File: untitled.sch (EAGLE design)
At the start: 21 parts

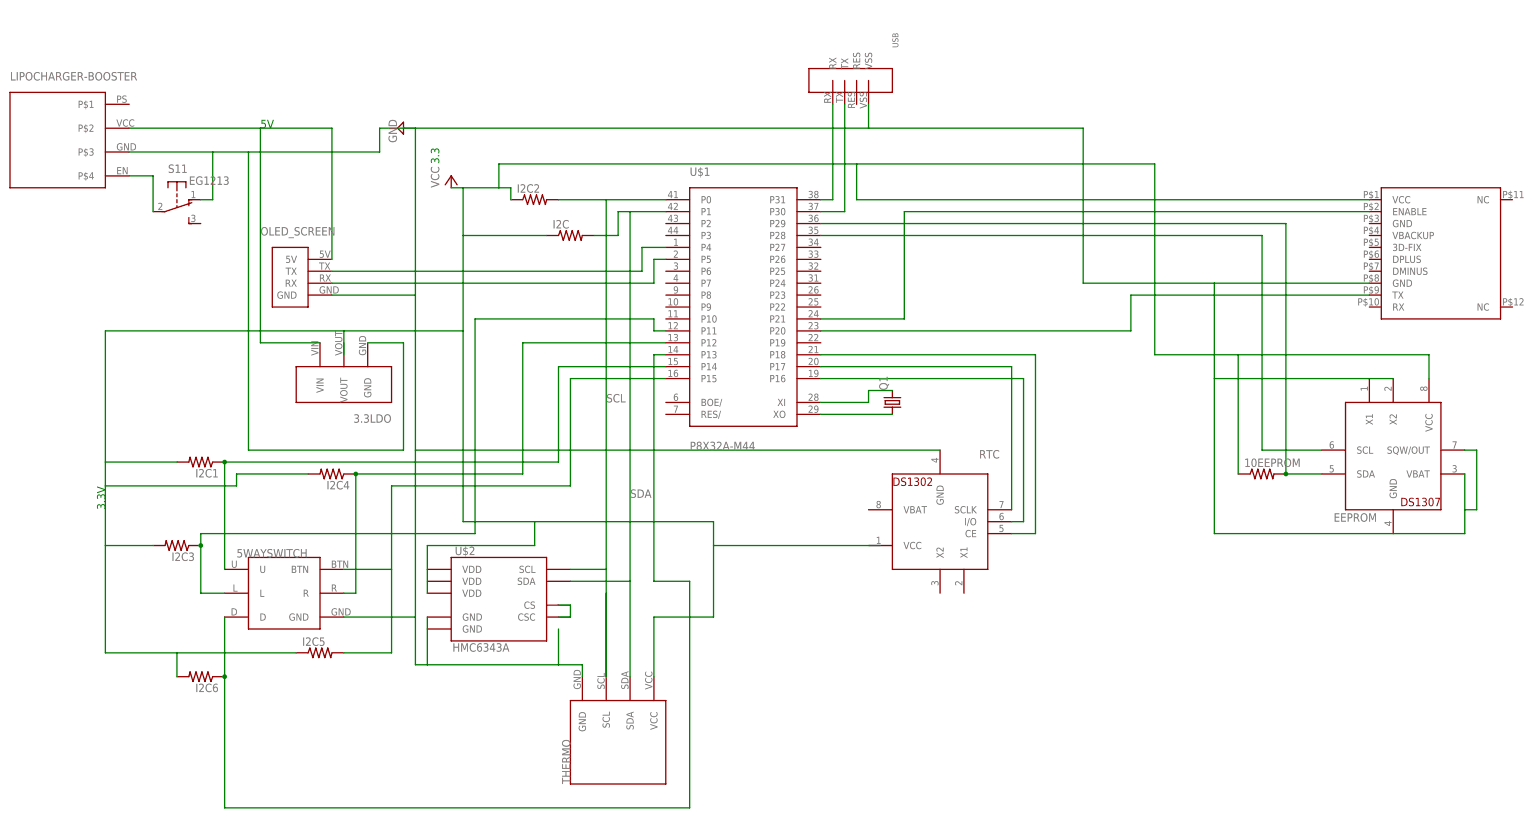
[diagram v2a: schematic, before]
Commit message: Add missing junctions to schematic
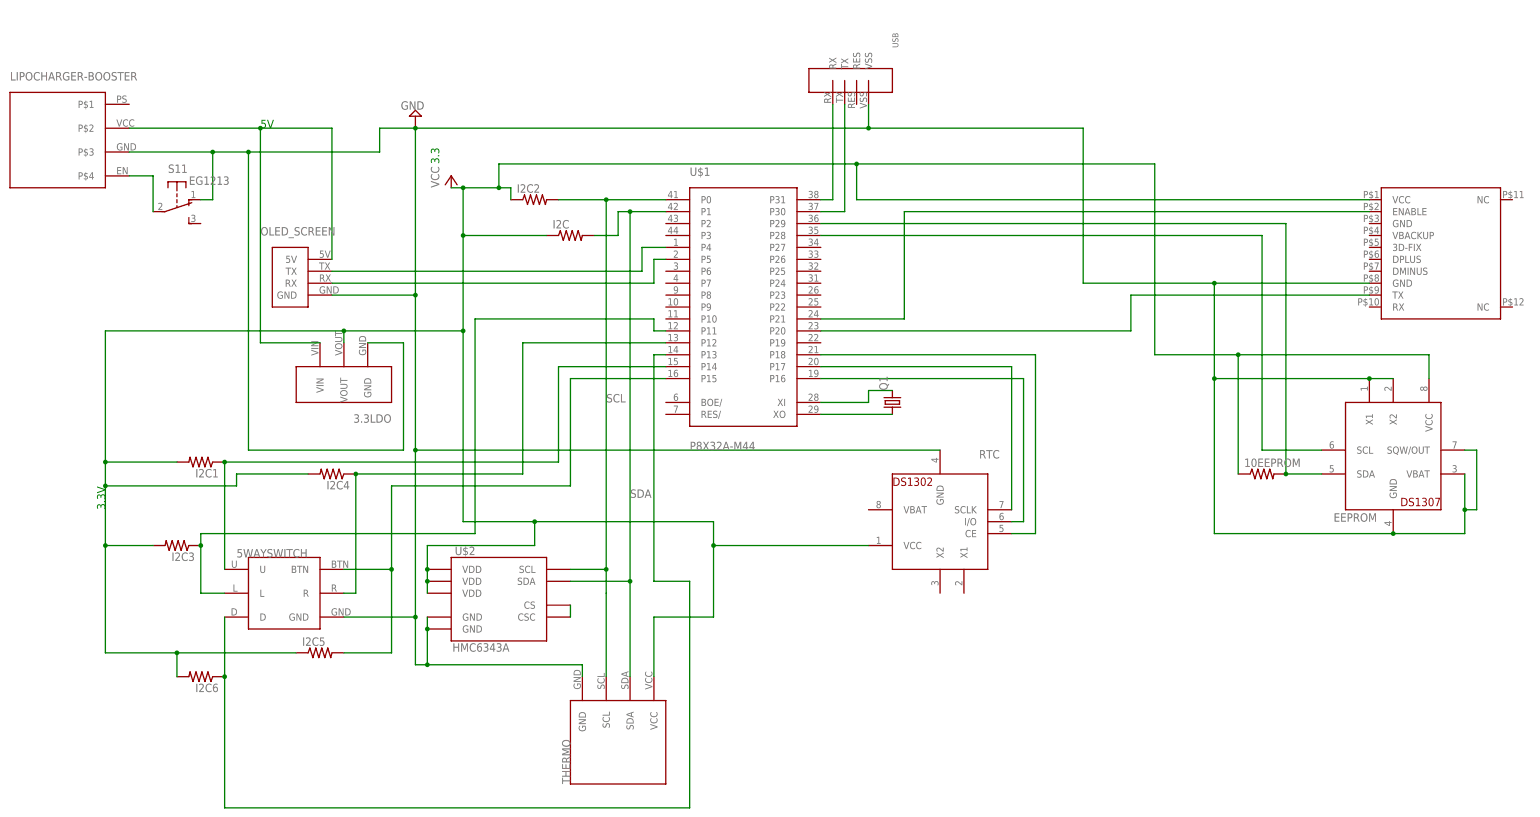
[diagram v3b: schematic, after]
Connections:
- net VCC: now also U$2.VDD@21
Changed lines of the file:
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@@
 <instance part="U$1" gate="G$1" x="25.4" y="63.5"/>
 <instance part="RTC" gate="G$1" x="68.58" y="15.24" rot="R180"/>
-<instance part="SUPPLY2" gate="GND" x="-45.72" y="99.06" rot="R270"/>
+<instance part="SUPPLY2" gate="GND" x="-43.18" y="101.6" rot="R180"/>
 <instance part="THERMO" gate="G$1" x="2.54" y="-30.48" rot="R90"/>
 <instance part="P+1" gate="VCC" x="-35.56" y="88.9"/>
@@
 <wire x1="-43.18" y1="-5.08" x2="-43.18" y2="-15.24" width="0.1524" layer="91"/>
 <wire x1="-43.18" y1="-15.24" x2="-40.64" y2="-15.24" width="0.1524" layer="91"/>
-<wire x1="-40.64" y1="-15.24" x2="-12.7" y2="-15.24" width="0.1524" layer="91"/>
-<wire x1="-12.7" y1="-15.24" x2="-12.7" y2="-7.62" width="0.1524" layer="91"/>
-<wire x1="-12.7" y1="-15.24" x2="-7.62" y2="-15.24" width="0.1524" layer="91"/>
+<wire x1="-40.64" y1="-15.24" x2="-7.62" y2="-15.24" width="0.1524" layer="91"/>
 <wire x1="-7.62" y1="-15.24" x2="-7.62" y2="-17.78" width="0.1524" layer="91"/>
 <pinref part="RTC" gate="G$1" pin="GND"/>
@@
 <pinref part="U$2" gate="G$1" pin="GND@25"/>
 <wire x1="-40.64" y1="-7.62" x2="-40.64" y2="-5.08" width="0.1524" layer="91"/>
+<junction x="-40.64" y="-7.62"/>
+<junction x="-40.64" y="-15.24"/>
+<junction x="-43.18" y="30.48"/>
+<junction x="160.02" y="45.72"/>
+<junction x="180.34" y="17.78"/>
+<junction x="-78.74" y="93.98"/>
+<junction x="-86.36" y="93.98"/>
+<junction x="53.34" y="99.06"/>
+<junction x="165.1" y="12.7"/>
+<junction x="-43.18" y="99.06"/>
+<junction x="-43.18" y="-5.08"/>
+<junction x="127" y="66.04"/>
+<junction x="-43.18" y="63.5"/>
+<junction x="127" y="45.72"/>
 </segment>
 </net>
@@
 <label x="-2.54" y="40.64" size="1.778" layer="95"/>
 <pinref part="THERMO" gate="G$1" pin="SCL"/>
-<wire x1="-2.54" y1="5.08" x2="-2.54" y2="-17.78" width="0.1524" layer="91"/>
+<wire x1="-2.54" y1="5.08" x2="-2.54" y2="0" width="0.1524" layer="91"/>
 <wire x1="-2.54" y1="0" x2="-2.54" y2="-17.78" width="0.1524" layer="91"/>
 <pinref part="I2C2" gate="G$1" pin="2"/>
 <pinref part="U$2" gate="G$1" pin="SCL"/>
 <wire x1="-10.16" y1="5.08" x2="-2.54" y2="5.08" width="0.1524" layer="91"/>
+<junction x="-2.54" y="83.82"/>
+<junction x="-2.54" y="5.08"/>
 </segment>
 </net>
@@
 <pinref part="U$2" gate="G$1" pin="SDA"/>
 <wire x1="-10.16" y1="2.54" x2="2.54" y2="2.54" width="0.1524" layer="91"/>
+<junction x="2.54" y="2.54"/>
+<junction x="2.54" y="81.28"/>
 </segment>
 </net>
@@
 <wire x1="20.32" y1="-5.08" x2="7.62" y2="-5.08" width="0.1524" layer="91"/>
 <wire x1="7.62" y1="-17.78" x2="7.62" y2="-5.08" width="0.1524" layer="91"/>
-<wire x1="55.88" y1="10.16" x2="20.32" y2="10.16" width="0.1524" layer="91"/>
+<wire x1="53.34" y1="10.16" x2="20.32" y2="10.16" width="0.1524" layer="91"/>
 <pinref part="THERMO" gate="G$1" pin="VCC"/>
 <pinref part="P+1" gate="VCC" pin="VCC"/>
@@
 <wire x1="-25.4" y1="91.44" x2="50.8" y2="91.44" width="0.1524" layer="91"/>
 <wire x1="50.8" y1="91.44" x2="50.8" y2="83.82" width="0.1524" layer="91"/>
-<wire x1="-58.42" y1="50.8" x2="-58.42" y2="55.88" width="0.1524" layer="91"/>
+<wire x1="-58.42" y1="53.34" x2="-58.42" y2="55.88" width="0.1524" layer="91"/>
 <wire x1="-58.42" y1="55.88" x2="-33.02" y2="55.88" width="0.1524" layer="91"/>
 <pinref part="GPS" gate="G$1" pin="VCC"/>
@@
 <pinref part="U$2" gate="G$1" pin="VDD@11"/>
 <pinref part="U$2" gate="G$1" pin="VDD@3"/>
-<wire x1="-40.64" y1="0" x2="-40.64" y2="5.08" width="0.1524" layer="91"/>
+<wire x1="-40.64" y1="0" x2="-40.64" y2="2.54" width="0.1524" layer="91"/>
+<wire x1="-40.64" y1="2.54" x2="-40.64" y2="5.08" width="0.1524" layer="91"/>
 <wire x1="-40.64" y1="5.08" x2="-40.64" y2="10.16" width="0.1524" layer="91"/>
 <wire x1="-40.64" y1="10.16" x2="-17.78" y2="10.16" width="0.1524" layer="91"/>
 <wire x1="-17.78" y1="10.16" x2="-17.78" y2="15.24" width="0.1524" layer="91"/>
+<junction x="-17.78" y="15.24"/>
+<junction x="-109.22" y="10.16"/>
+<junction x="132.08" y="50.8"/>
+<junction x="50.8" y="91.44"/>
+<junction x="-33.02" y="76.2"/>
+<junction x="-33.02" y="55.88"/>
+<junction x="-40.64" y="5.08"/>
+<junction x="-58.42" y="55.88"/>
+<junction x="20.32" y="10.16"/>
+<junction x="-109.22" y="27.94"/>
+<junction x="-33.02" y="86.36"/>
+<junction x="-25.4" y="86.36"/>
+<junction x="-109.22" y="22.86"/>
+<junction x="-93.98" y="-12.7"/>
+<pinref part="U$2" gate="G$1" pin="VDD@21"/>
+<junction x="-40.64" y="2.54"/>
 </segment>
 </net>
@@
 <pinref part="3.3LDO" gate="G$1" pin="VIN"/>
 <wire x1="-76.2" y1="53.34" x2="-63.5" y2="53.34" width="0.1524" layer="91"/>
+<junction x="-76.2" y="99.06"/>
 </segment>
 </net>
@@
 <wire x1="-58.42" y1="-12.7" x2="-48.26" y2="-12.7" width="0.1524" layer="91"/>
 <wire x1="-48.26" y1="-12.7" x2="-48.26" y2="5.08" width="0.1524" layer="91"/>
+<junction x="-48.26" y="5.08"/>
 </segment>
 </net>
 <net name="N$22" class="0">
 <segment>
-<wire x1="-12.7" y1="-2.54" x2="-10.16" y2="-2.54" width="0.1524" layer="91"/>
 <pinref part="U$2" gate="G$1" pin="CS"/>
-<wire x1="-10.16" y1="-5.08" x2="-12.7" y2="-5.08" width="0.1524" layer="91"/>
 <pinref part="U$2" gate="G$1" pin="CSC"/>
 <wire x1="-10.16" y1="-2.54" x2="-10.16" y2="-5.08" width="0.1524" layer="91"/>

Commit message: Add supply symbols, didn't fix board
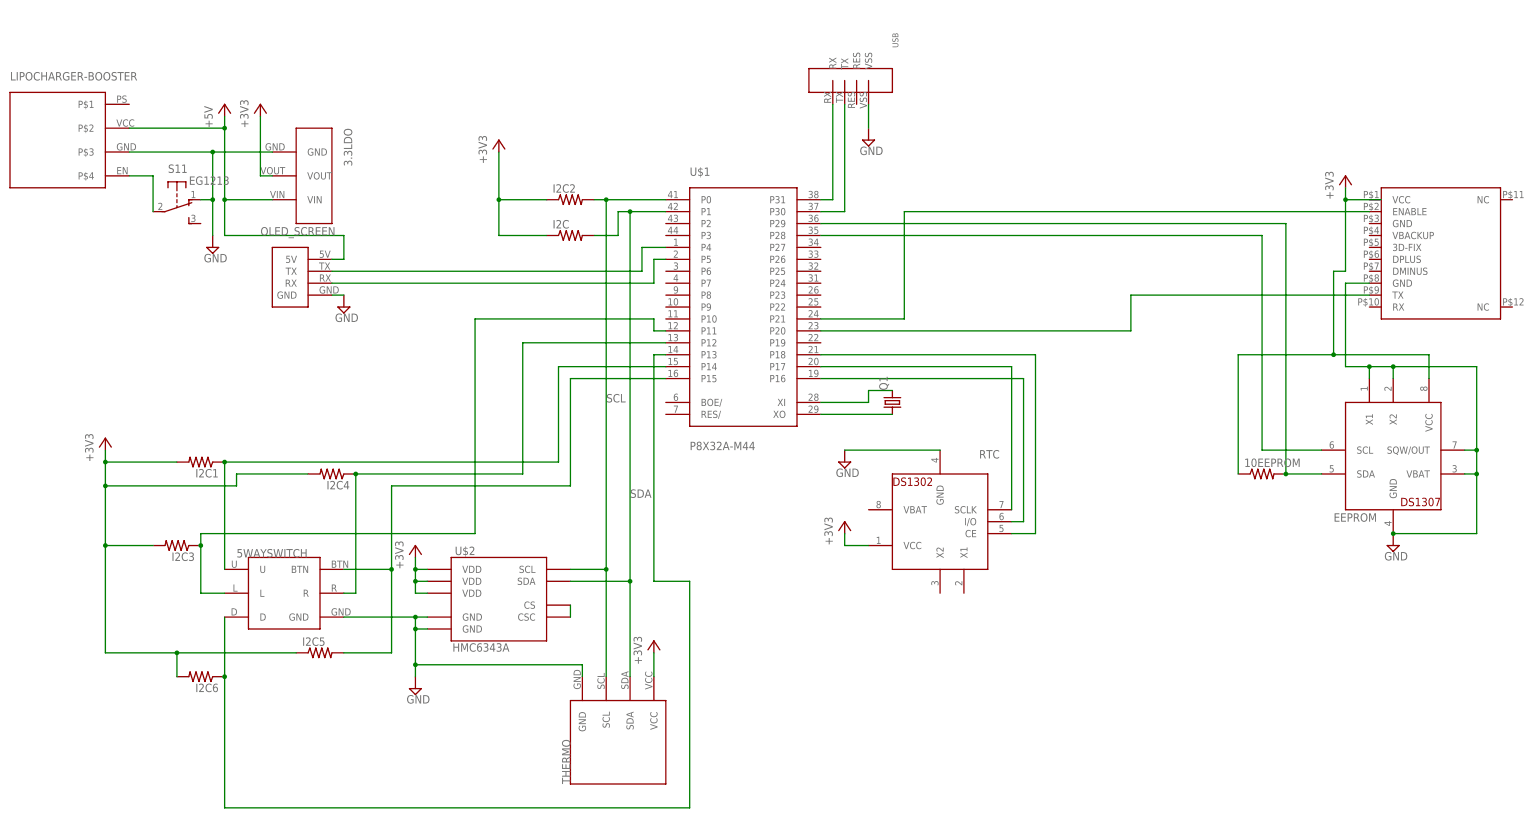
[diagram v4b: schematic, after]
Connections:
- net N$12 renamed +5V
- removed net VCC: 10EEPROM.1, EEPROM.VCC, GPS.VCC, I2C.1, I2C1.2, I2C2.1, I2C3.2, I2C4.2, I2C5.1, I2C6.2, THERMO.VCC, U$2.VDD@11, U$2.VDD@21, U$2.VDD@3
- new net +3V3: 10EEPROM.1, 3.3LDO.VOUT, EEPROM.VCC, I2C.1, I2C1.2, I2C2.1, I2C3.2, I2C4.2, I2C5.1, I2C6.2, RTC.VCC, THERMO.VCC, U$2.VDD@11, U$2.VDD@21, U$2.VDD@3
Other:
- note removed: "3.3"
- note removed: "3.3V"
- note removed: "5V"
- moved on the sheet: 3.3LDO, I2C2

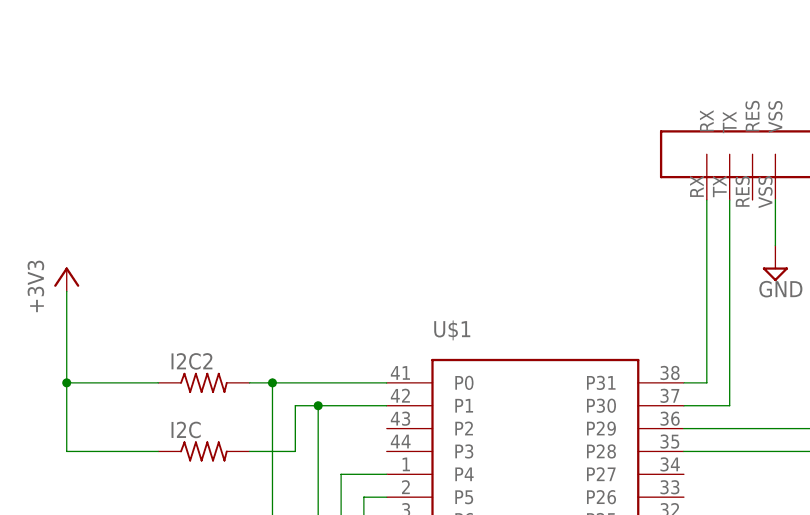
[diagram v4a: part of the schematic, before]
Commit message: Added power and decoupling caps to schematic
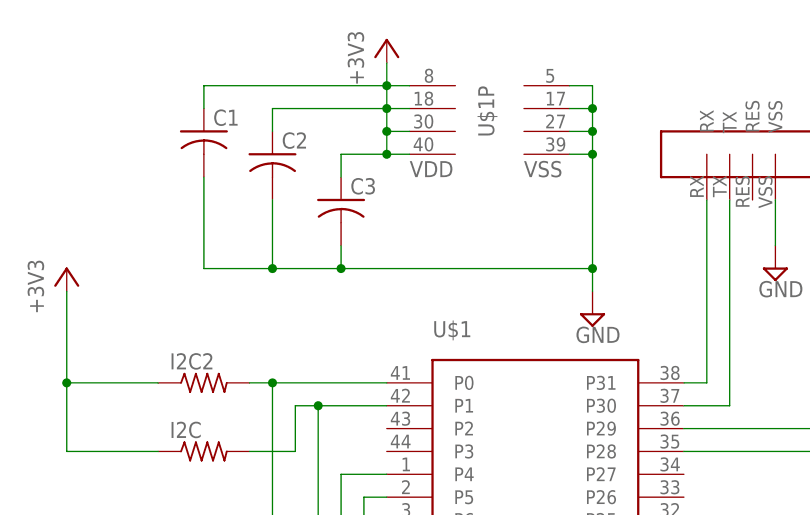
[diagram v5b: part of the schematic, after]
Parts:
- added C1, C2, C3: (no value), rcl:C-USC0603
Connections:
- net +3V3: now also C1.1, C2.1, C3.1, U$1P.VDD@1, U$1P.VDD@2, U$1P.VDD@3, U$1P.VDD@4
- net GND: now also C1.2, C2.2, C3.2, U$1P.VSS@1, U$1P.VSS@2, U$1P.VSS@3, U$1P.VSS@4
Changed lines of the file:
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@@
 <part name="+3V6" library="supply1" deviceset="+3V3" device=""/>
 <part name="+3V7" library="supply1" deviceset="+3V3" device=""/>
+<part name="SUPPLY7" library="supply2" deviceset="GND" device=""/>
+<part name="+3V8" library="supply1" deviceset="+3V3" device=""/>
+<part name="C1" library="rcl" deviceset="C-US" device="C0603"/>
+<part name="C2" library="rcl" deviceset="C-US" device="C0603"/>
+<part name="C3" library="rcl" deviceset="C-US" device="C0603"/>
 </parts>
 <sheets>
@@
 <instance part="+3V6" gate="G$1" x="48.26" y="15.24"/>
 <instance part="+3V7" gate="G$1" x="154.94" y="88.9"/>
+<instance part="U$1" gate="P" x="20.32" y="111.76"/>
+<instance part="SUPPLY7" gate="GND" x="33.02" y="91.44"/>
+<instance part="+3V8" gate="G$1" x="10.16" y="121.92"/>
+<instance part="C1" gate="G$1" x="-10.16" y="111.76"/>
+<instance part="C2" gate="G$1" x="-2.54" y="109.22"/>
+<instance part="C3" gate="G$1" x="5.08" y="104.14"/>
 </instances>
 <busses>
@@
 <junction x="160.02" y="48.26"/>
 </segment>
+<segment>
+<pinref part="U$1" gate="P" pin="VSS@4"/>
+<pinref part="SUPPLY7" gate="GND" pin="GND"/>
+<wire x1="30.48" y1="109.22" x2="33.02" y2="109.22" width="0.1524" layer="91"/>
+<wire x1="33.02" y1="109.22" x2="33.02" y2="96.52" width="0.1524" layer="91"/>
+<pinref part="U$1" gate="P" pin="VSS@3"/>
+<wire x1="33.02" y1="96.52" x2="33.02" y2="93.98" width="0.1524" layer="91"/>
+<wire x1="30.48" y1="111.76" x2="33.02" y2="111.76" width="0.1524" layer="91"/>
+<wire x1="33.02" y1="111.76" x2="33.02" y2="109.22" width="0.1524" layer="91"/>
+<junction x="33.02" y="109.22"/>
+<pinref part="U$1" gate="P" pin="VSS@2"/>
+<wire x1="30.48" y1="114.3" x2="33.02" y2="114.3" width="0.1524" layer="91"/>
+<wire x1="33.02" y1="114.3" x2="33.02" y2="111.76" width="0.1524" layer="91"/>
+<junction x="33.02" y="111.76"/>
+<pinref part="U$1" gate="P" pin="VSS@1"/>
+<wire x1="30.48" y1="116.84" x2="33.02" y2="116.84" width="0.1524" layer="91"/>
+<wire x1="33.02" y1="116.84" x2="33.02" y2="114.3" width="0.1524" layer="91"/>
+<junction x="33.02" y="114.3"/>
+<pinref part="C3" gate="G$1" pin="2"/>
+<wire x1="5.08" y1="99.06" x2="5.08" y2="96.52" width="0.1524" layer="91"/>
+<wire x1="5.08" y1="96.52" x2="33.02" y2="96.52" width="0.1524" layer="91"/>
+<pinref part="C2" gate="G$1" pin="2"/>
+<wire x1="-2.54" y1="104.14" x2="-2.54" y2="96.52" width="0.1524" layer="91"/>
+<wire x1="-2.54" y1="96.52" x2="5.08" y2="96.52" width="0.1524" layer="91"/>
+<junction x="5.08" y="96.52"/>
+<pinref part="C1" gate="G$1" pin="2"/>
+<wire x1="-10.16" y1="106.68" x2="-10.16" y2="96.52" width="0.1524" layer="91"/>
+<wire x1="-10.16" y1="96.52" x2="-2.54" y2="96.52" width="0.1524" layer="91"/>
+<junction x="-2.54" y="96.52"/>
+<junction x="33.02" y="96.52"/>
+</segment>
 </net>
 <net name="+5V" class="0">
@@
 <pinref part="+3V3" gate="G$1" pin="+3V3"/>
 </segment>
-</net>
+<segment>
+<pinref part="U$1" gate="P" pin="VDD@1"/>
+<pinref part="+3V8" gate="G$1" pin="+3V3"/>
+<wire x1="12.7" y1="116.84" x2="10.16" y2="116.84" width="0.1524" layer="91"/>
+<wire x1="10.16" y1="116.84" x2="10.16" y2="119.38" width="0.1524" layer="91"/>
+<pinref part="U$1" gate="P" pin="VDD@2"/>
+<wire x1="12.7" y1="114.3" x2="10.16" y2="114.3" width="0.1524" layer="91"/>
+<wire x1="10.16" y1="114.3" x2="10.16" y2="116.84" width="0.1524" layer="91"/>
+<junction x="10.16" y="116.84"/>
+<pinref part="U$1" gate="P" pin="VDD@3"/>
+<wire x1="12.7" y1="111.76" x2="10.16" y2="111.76" width="0.1524" layer="91"/>
+<wire x1="10.16" y1="111.76" x2="10.16" y2="114.3" width="0.1524" layer="91"/>
+<junction x="10.16" y="114.3"/>
+<pinref part="U$1" gate="P" pin="VDD@4"/>
+<wire x1="12.7" y1="109.22" x2="10.16" y2="109.22" width="0.1524" layer="91"/>
+<wire x1="10.16" y1="109.22" x2="10.16" y2="111.76" width="0.1524" layer="91"/>
+<junction x="10.16" y="111.76"/>
+<pinref part="C1" gate="G$1" pin="1"/>
+<wire x1="-10.16" y1="114.3" x2="-10.16" y2="116.84" width="0.1524" layer="91"/>
+<wire x1="-10.16" y1="116.84" x2="10.16" y2="116.84" width="0.1524" layer="91"/>
+<pinref part="C2" gate="G$1" pin="1"/>
+<wire x1="-2.54" y1="111.76" x2="-2.54" y2="114.3" width="0.1524" layer="91"/>
+<wire x1="-2.54" y1="114.3" x2="10.16" y2="114.3" width="0.1524" layer="91"/>
+<pinref part="C3" gate="G$1" pin="1"/>
+<wire x1="5.08" y1="106.68" x2="5.08" y2="109.22" width="0.1524" layer="91"/>
+<wire x1="5.08" y1="109.22" x2="10.16" y2="109.22" width="0.1524" layer="91"/>
+<junction x="10.16" y="109.22"/>
+</segment>
+</net>
